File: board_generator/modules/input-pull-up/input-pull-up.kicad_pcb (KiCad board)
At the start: 2 copper layers, 11.4 x 20.3 mm, 6 parts, among them J1 Screw_Terminal_1x01, X1 interface, X2 interface

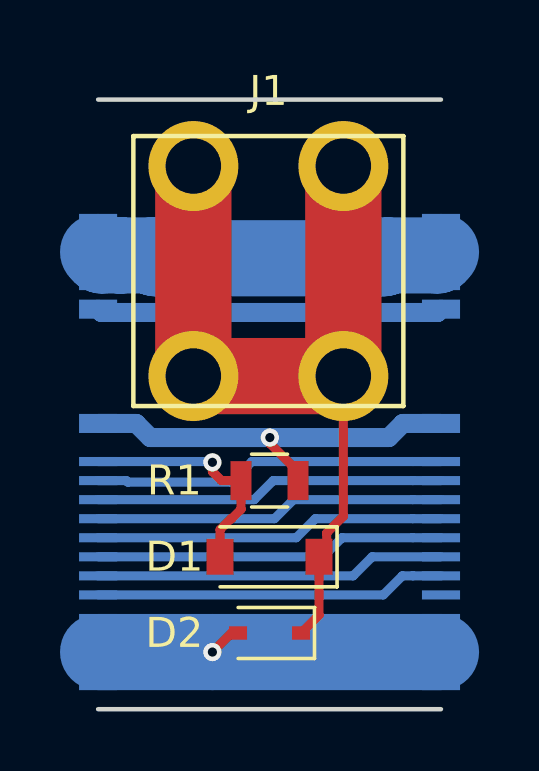
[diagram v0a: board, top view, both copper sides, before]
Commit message: Using solder pads for module input_pull_up
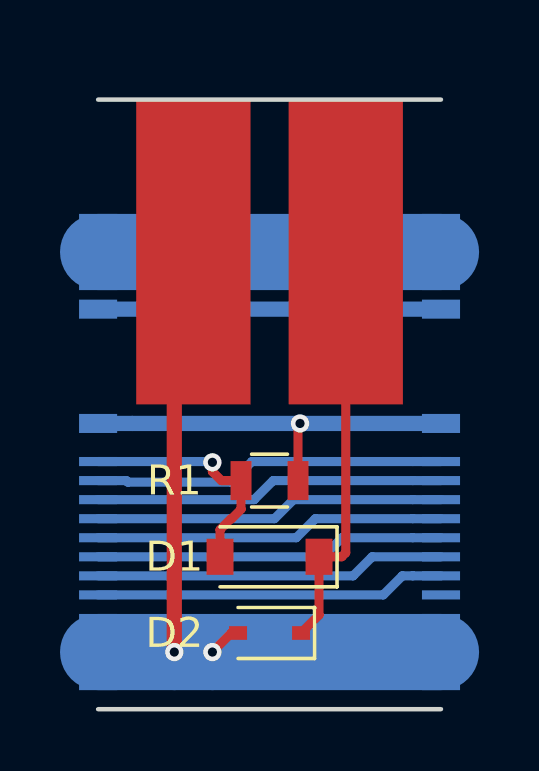
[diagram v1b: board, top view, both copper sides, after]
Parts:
- added J2: GND, connectors:SolderWirePad_single_SMD_15x40mil, F.Cu at (140.3, 109.2)
- J1: value Screw_Terminal_1x01 -> IN; footprint connectors:TERM_SCREW_M3 -> connectors:SolderWirePad_single_SMD_15x40mil
- R1: value R -> 10k
- moved J1 2.66 mm to (145.4, 109.2)
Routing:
- net Net-(D1-Pad1): track 28.3 -> 14.0 mm
- net GND: track 12.5 -> 26.1 mm, vias 1 -> 2
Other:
- board text added: "GND"
- board text added: "IN"
